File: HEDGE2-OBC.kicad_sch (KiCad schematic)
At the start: 36 parts, among them J1 SMA-J-P-X-RA-TH1, U1 ADP7158ARDZ-3.3-R7, U3 TXS0102QDCURQ1

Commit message: Arbitrary change for demo purposes
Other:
- note added: "arvitrary text"
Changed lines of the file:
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@@
+		)
+	)
+	(text "arvitrary text"
+		(exclude_from_sim no)
+		(at 119.634 144.526 0)
+		(effects
+			(font
+				(size 1.27 1.27)
+			)
 		)
 	)

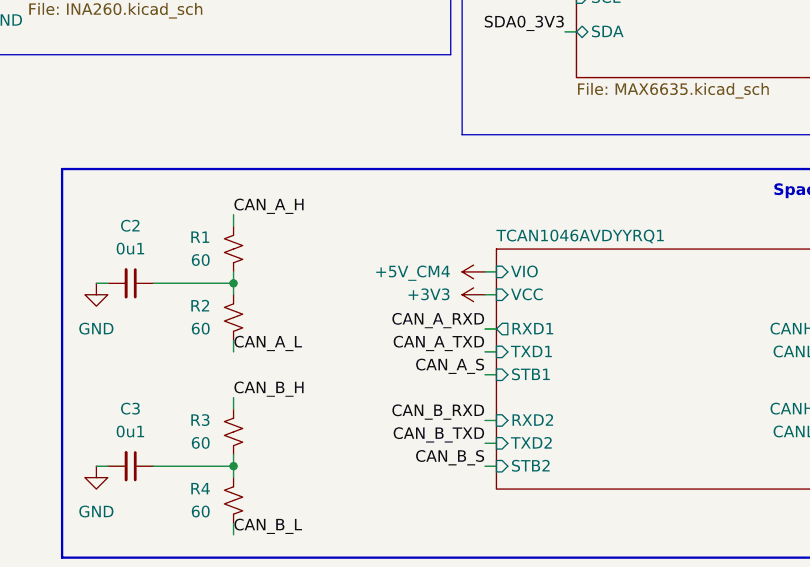
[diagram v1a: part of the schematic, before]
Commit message: Fix TCAN power supply swap
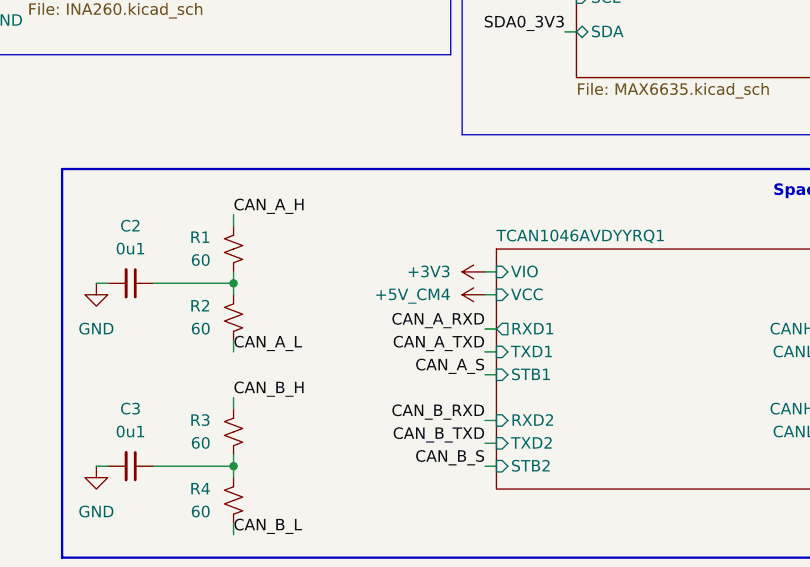
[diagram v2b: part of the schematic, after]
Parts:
- C1, C5, C6: DigiKey Part Number (none) -> 1276-1029-1-ND
- C7, C8: DigiKey Part Number (none) -> 720-GA0805Y104JXABT31GCT-ND
- MH1, MH2, MH3, MH4: now left out of the parts list
- R10, R11, R20, R21: DigiKey Part Number RMCF0805JT47K0CT-ND -> 541-4131-1-ND
- R5: DigiKey Part Number (none) -> 541-10.0KCCT-ND
- R6, R7: DigiKey Part Number 541-2.10KCCT-ND -> 541-1.00KCCT-ND
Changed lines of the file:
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@@
 			)
 		)
-		(property "DigiKey Part Number" "RMCF0805JT47K0CT-ND"
+		(property "DigiKey Part Number" "541-4131-1-ND "
 			(at 308.61 194.31 0)
 			(effects
@@
 			)
 		)
+		(property "DigiKey Part Number" "1276-1029-1-ND"
+			(at 123.19 251.46 0)
+			(effects
+				(font
+					(size 1.27 1.27)
+				)
+				(hide yes)
+			)
+		)
 		(pin "1"
 		)
@@
 	(symbol
 		(lib_id "power:+5V")
-		(at 163.83 95.25 90)
+		(at 163.83 97.79 90)
 		(unit 1)
 		(exclude_from_sim no)
@@
 		(on_board yes)
 		(dnp no)
-		(fields_autoplaced yes)
 		(property "Reference" "#PWR033"
-			(at 167.64 95.25 0)
+			(at 167.64 97.79 0)
 			(effects
 				(font
@@
 		)
 		(property "Value" "+5V_CM4"
-			(at 160.02 95.2499 90)
+			(at 160.02 97.7899 90)
 			(effects
 				(font
@@
 		)
 		(property "Footprint" ""
-			(at 163.83 95.25 0)
+			(at 163.83 97.79 0)
 			(effects
 				(font
@@
 		)
 		(property "Datasheet" ""
-			(at 163.83 95.25 0)
+			(at 163.83 97.79 0)
 			(effects
 				(font
@@
 		)
 		(property "Description" "Power symbol creates a global label with name \"+5V\""
-			(at 163.83 95.25 0)
+			(at 163.83 97.79 0)
 			(effects
 				(font
@@
 			)
 		)
-		(property "DigiKey Part Number" "541-2.10KCCT-ND"
+		(property "DigiKey Part Number" "541-1.00KCCT-ND "
 			(at 327.66 144.78 0)
 			(effects
@@
 			)
 		)
-		(property "DigiKey Part Number" "RMCF0805JT47K0CT-ND"
+		(property "DigiKey Part Number" "541-4131-1-ND "
 			(at 308.61 185.42 0)
 			(effects
@@
 		(unit 1)
 		(exclude_from_sim no)
-		(in_bom yes)
+		(in_bom no)
 		(on_board yes)
 		(dnp no)
@@
 			)
 		)
+		(property "DigiKey Part Number" "720-GA0805Y104JXABT31GCT-ND"
+			(at 276.86 177.8 0)
+			(effects
+				(font
+					(size 1.27 1.27)
+				)
+				(hide yes)
+			)
+		)
 		(pin "1"
 		)
@@
 			)
 		)
+		(property "DigiKey Part Number" "1276-1029-1-ND"
+			(at 114.3 254 0)
+			(effects
+				(font
+					(size 1.27 1.27)
+				)
+				(hide yes)
+			)
+		)
 		(pin "1"
 		)
@@
 			)
 		)
-		(property "DigiKey Part Number" "541-2.10KCCT-ND"
+		(property "DigiKey Part Number" "541-1.00KCCT-ND "
 			(at 327.66 137.16 0)
 			(effects
@@
 			)
 		)
-		(property "DigiKey Part Number" "RMCF0805JT47K0CT-ND"
+		(property "DigiKey Part Number" "541-4131-1-ND "
 			(at 308.61 212.09 0)
 			(effects
@@
 			)
 		)
+		(property "DigiKey Part Number" "1276-1029-1-ND"
+			(at 17.78 251.46 0)
+			(effects
+				(font
+					(size 1.27 1.27)
+				)
+				(hide yes)
+			)
+		)
 		(pin "2"
 		)
@@
 			)
 		)
+		(property "DigiKey Part Number" "720-GA0805Y104JXABT31GCT-ND"
+			(at 276.86 190.5 0)
+			(effects
+				(font
+					(size 1.27 1.27)
+				)
+				(hide yes)
+			)
+		)
 		(pin "1"
 		)
@@
 	(symbol
 		(lib_id "power:+3V3")
-		(at 163.83 97.79 90)
+		(at 163.83 95.25 90)
 		(unit 1)
 		(exclude_from_sim no)
@@
 		(on_board yes)
 		(dnp no)
-		(fields_autoplaced yes)
 		(property "Reference" "#PWR034"
-			(at 167.64 97.79 0)
+			(at 167.64 95.25 0)
 			(effects
 				(font
@@
 		)
 		(property "Value" "+3V3"
-			(at 160.02 97.7899 90)
+			(at 160.02 95.2499 90)
 			(effects
 				(font
@@
 		)
 		(property "Footprint" ""
-			(at 163.83 97.79 0)
+			(at 163.83 95.25 0)
 			(effects
 				(font
@@
 		)
 		(property "Datasheet" ""
-			(at 163.83 97.79 0)
+			(at 163.83 95.25 0)
 			(effects
 				(font
@@
 		)
 		(property "Description" "Power symbol creates a global label with name \"+3V3\""
-			(at 163.83 97.79 0)
+			(at 163.83 95.25 0)
 			(effects
 				(font
@@
 		(unit 1)
 		(exclude_from_sim no)
-		(in_bom yes)
+		(in_bom no)
 		(on_board yes)
 		(dnp no)
@@
 		(unit 1)
 		(exclude_from_sim no)
-		(in_bom yes)
+		(in_bom no)
 		(on_board yes)
 		(dnp no)
@@
 		(unit 1)
 		(exclude_from_sim no)
-		(in_bom yes)
+		(in_bom no)
 		(on_board yes)
 		(dnp no)
@@
 			)
 		)
+		(property "DigiKey Part Number" "541-10.0KCCT-ND "
+			(at 238.76 184.15 0)
+			(effects
+				(font
+					(size 1.27 1.27)
+				)
+				(hide yes)
+			)
+		)
 		(pin "1"
 		)
@@
 			)
 		)
-		(property "DigiKey Part Number" "RMCF0805JT47K0CT-ND"
+		(property "DigiKey Part Number" "541-4131-1-ND "
 			(at 308.61 203.2 0)
 			(effects

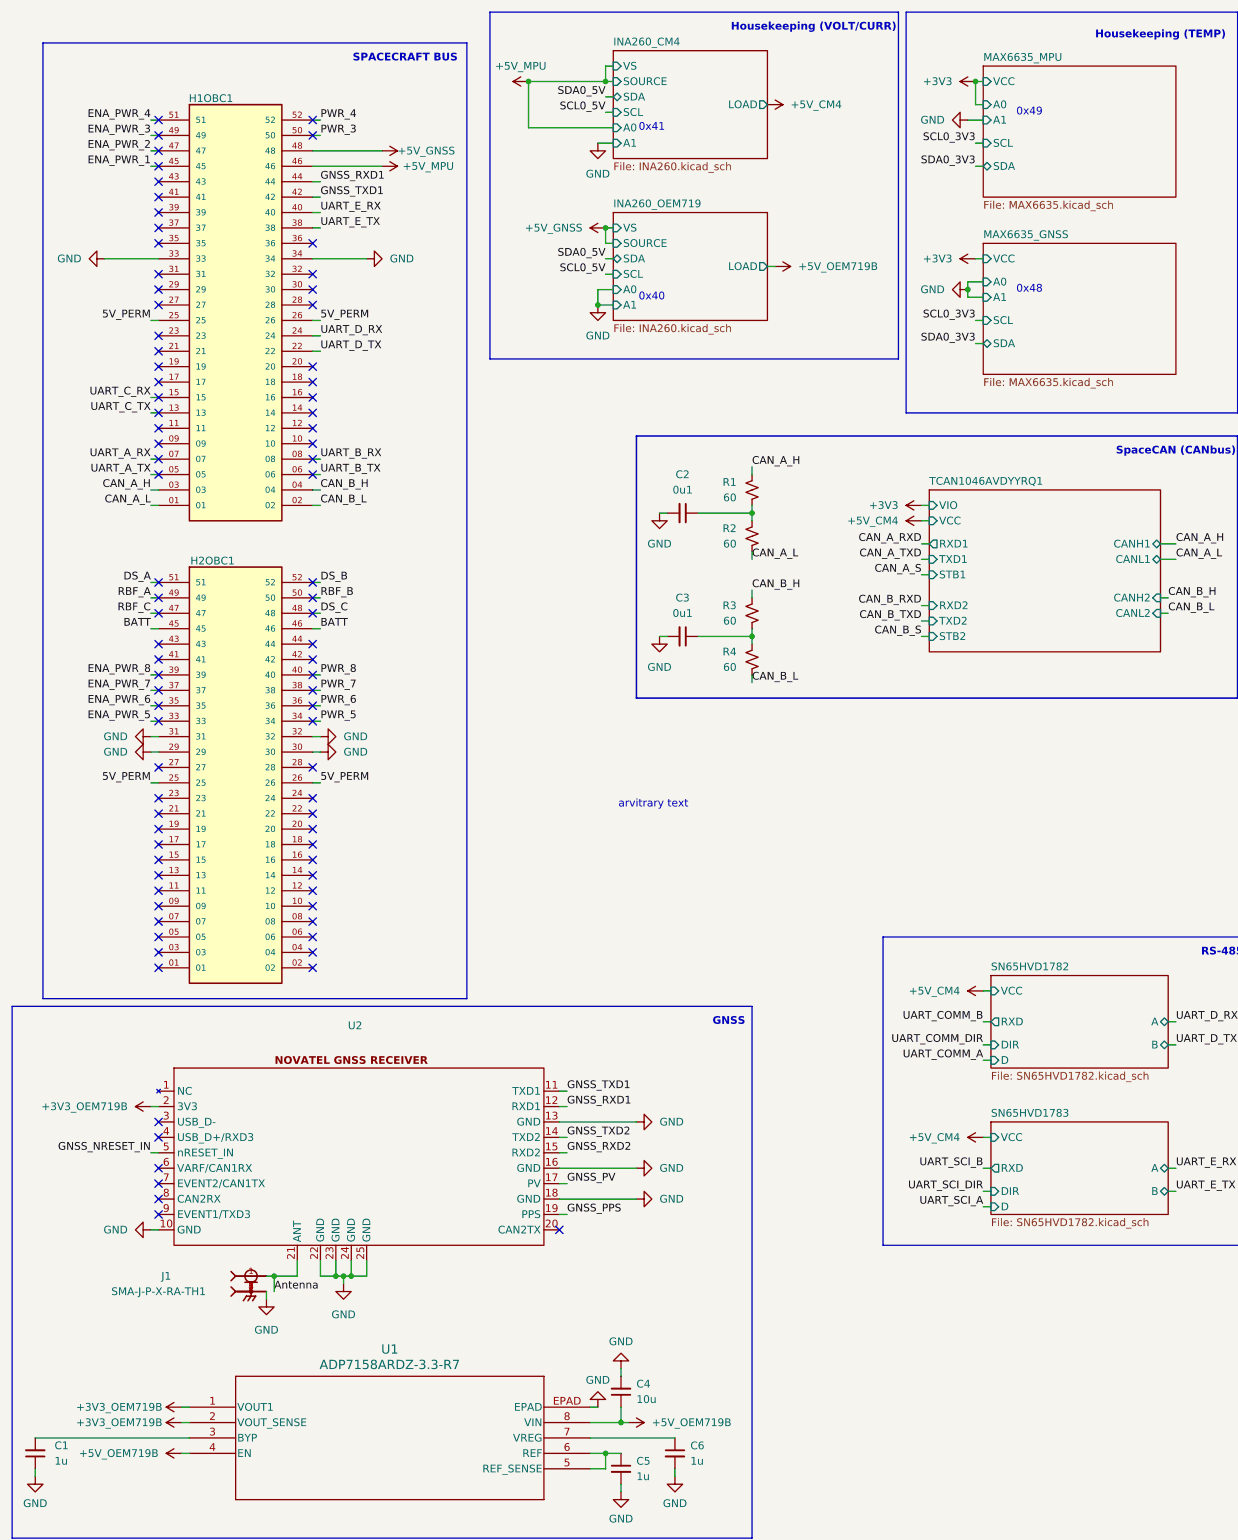
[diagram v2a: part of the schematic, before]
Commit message: Add cap to 3V3 LDO output; add solder jumpers; change 3V3 routing
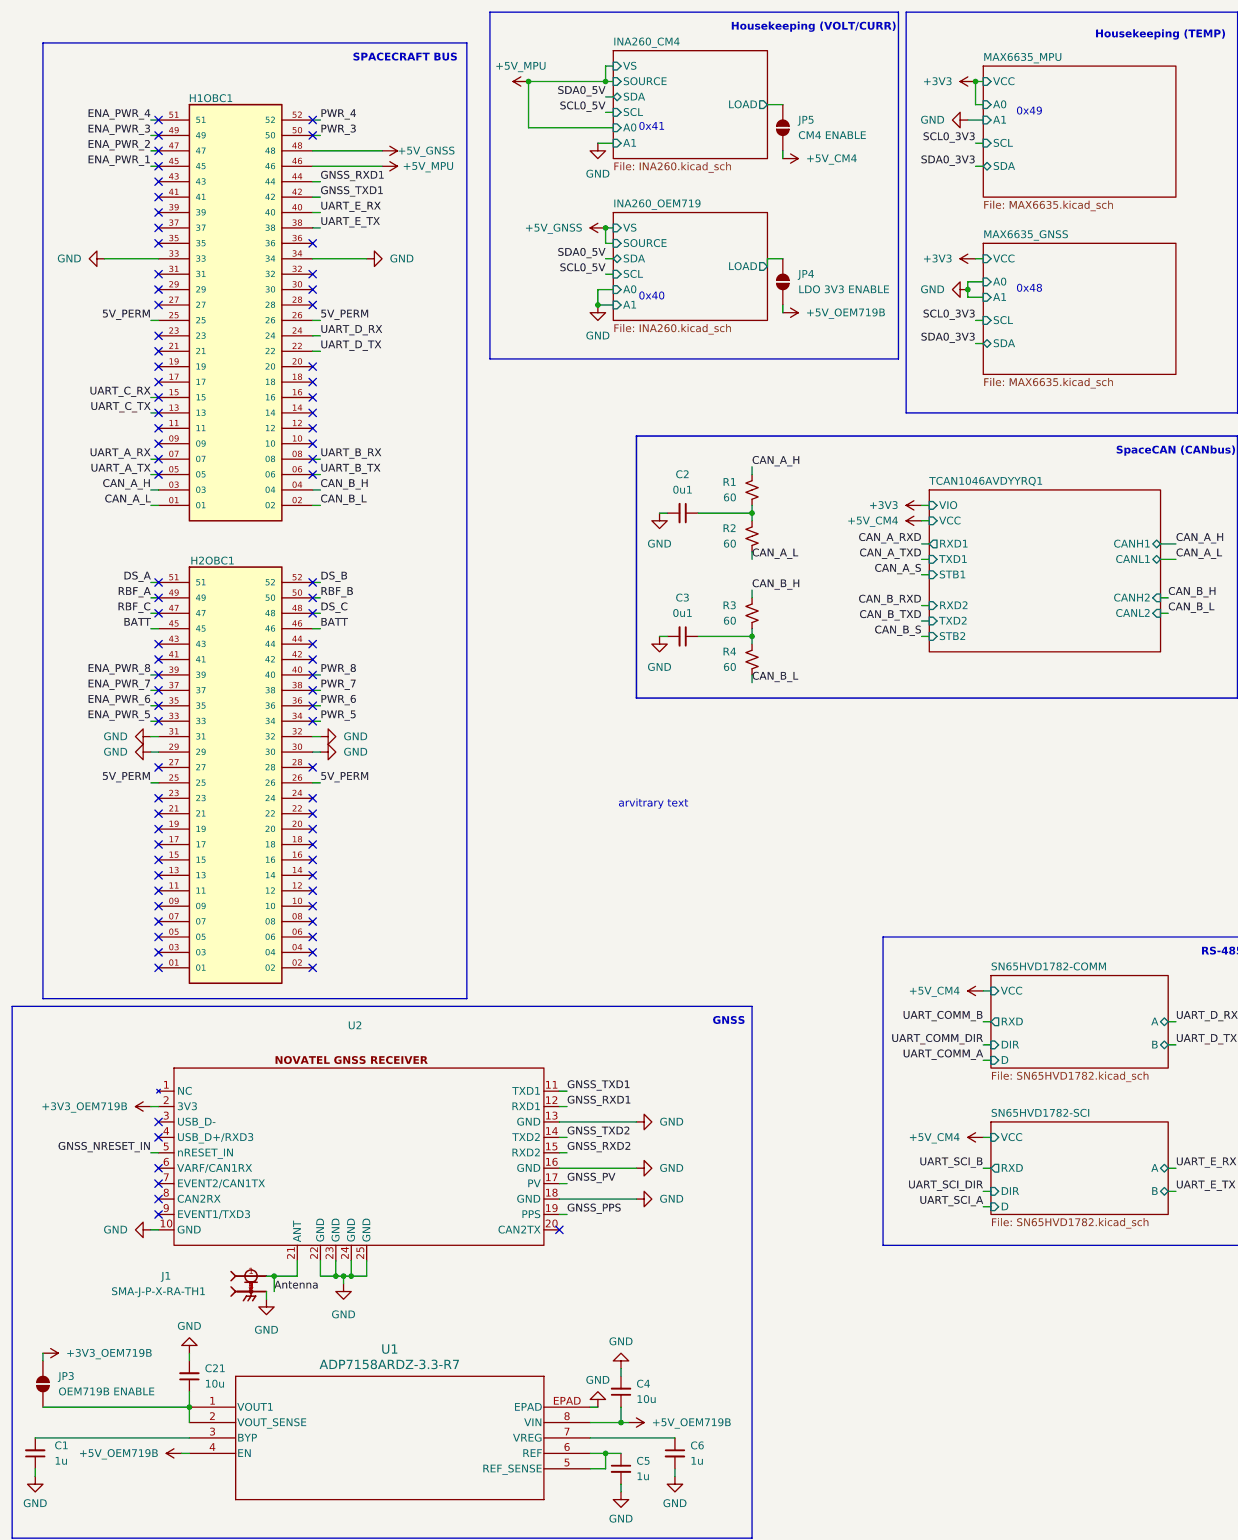
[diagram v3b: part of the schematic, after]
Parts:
- added C21: 10u, Capacitor_SMD:C_0805_2012Metric, symbol Device:C_Small
- added JP3: OEM719B ENABLE, Jumper:SolderJumper-2_P1.3mm_Open_RoundedPad1.0x1.5mm, symbol Jumper:SolderJumper_2_Open
- added JP4: LDO 3V3 ENABLE, Jumper:SolderJumper-2_P1.3mm_Open_RoundedPad1.0x1.5mm, symbol Jumper:SolderJumper_2_Open
- added JP5: CM4 ENABLE, Jumper:SolderJumper-2_P1.3mm_Open_RoundedPad1.0x1.5mm, symbol Jumper:SolderJumper_2_Open
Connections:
- net +3V3_OEM719B: now also JP3.2 (B); no longer U1.1 (VOUT1), U1.2 (VOUT_SENSE)
- net +5V_CM4: now also JP5.1 (A)
- net +5V_OEM719B: now also JP4.1 (A)
- net GND: now also C21.2
- new net: C21.1, JP3.1 (A), U1.1 (VOUT1), U1.2 (VOUT_SENSE)
- new net INA260_CM4/LOAD: JP5.2 (B)
- new net INA260_OEM719/LOAD: JP4.2 (B)
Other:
- sheet SN65HVD1782 renamed SN65HVD1782-COMM
- sheet SN65HVD1783 renamed SN65HVD1782-SCI

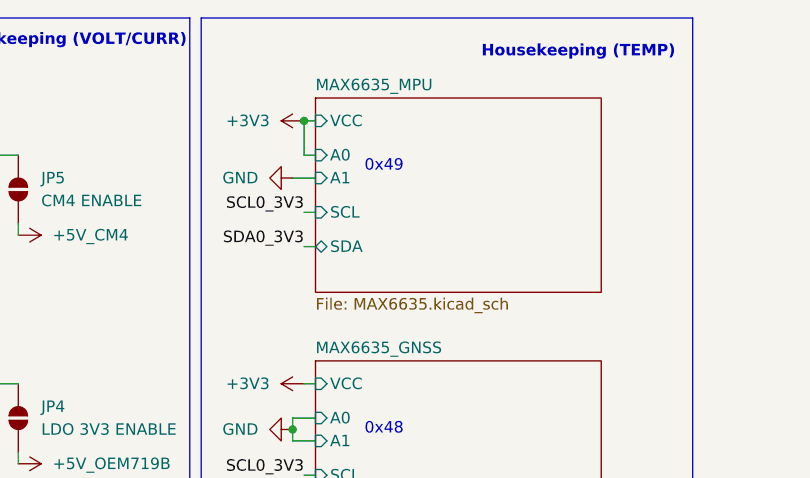
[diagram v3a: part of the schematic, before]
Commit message: Clean up CM4 routing
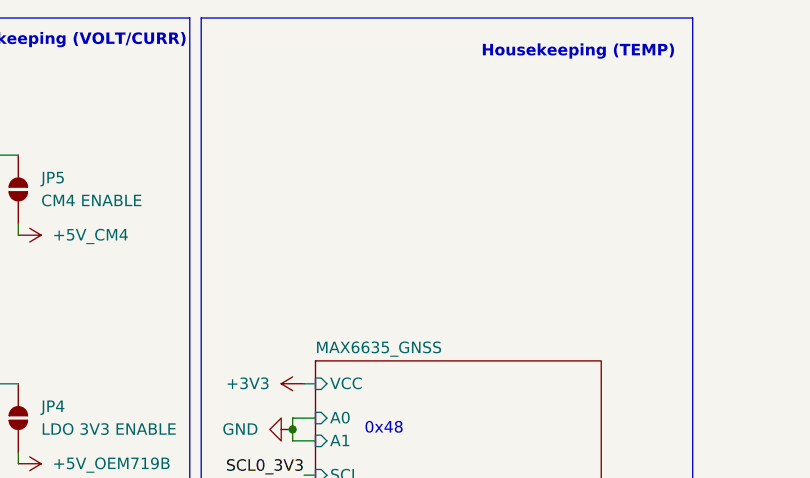
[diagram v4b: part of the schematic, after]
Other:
- removed sheet MAX6635_MPU
- note removed: "0x49"

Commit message: Add PCM5102A I2S audio output for APRS radio
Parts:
- removed JP1: WiFi_nDisable, Jumper:SolderJumper-2_P1.3mm_Open_RoundedPad1.0x1.5mm, symbol Jumper:SolderJumper_2_Open
- removed JP2: BT_nDisable, Jumper:SolderJumper-2_P1.3mm_Bridged2Bar_RoundedPad1.0x1.5mm, symbol Jumper:SolderJumper_2_Bridged
- removed R6, R7: 1k, Resistor_SMD:R_0805_2012Metric, symbol Device:R_Small_US
- added C10, C7: 2u2, Capacitor_SMD:C_0805_2012Metric, symbol Device:C_Small
- added C11, C12, C18, C19: 0u1, Capacitor_SMD:C_0805_2012Metric, symbol Device:C_Small
- added C17, C20, C8, C9: 10u, Capacitor_Tantalum_SMD:CP_EIA-2012-12_Kemet-R, symbol Device:C_Polarized_Small_US
- added C6: 2n2, Capacitor_SMD:C_0805_2012Metric, symbol Device:C_Small
- added R1: 470, Resistor_SMD:R_0805_2012Metric, symbol Device:R_Small_US
- added U3: SN74CBTLV3257PWR, SN74CBTLV3257PWR:PW16, symbol SN74CBTLV3257PWR:SN74CBTLV3257PWR
- added U4: PCM5102AQPWRQ1, PCM5102AQPWRQ1:PW20, symbol PCM5102AQPWRQ1:PCM5102AQPWRQ1
- renumbered C2 to C13, C3 to C14, C7 to C15, C8 to C16, C21 to C2, C4 to C3, C5 to C4, C6 to C5, JP3 to JP1, JP5 to JP2, JP4 to JP3, R11 to R10, R8 to R11, R9 to R12, R5 to R2, R1 to R3, R2 to R4, R3 to R5, R4 to R6, R20 to R7, R21 to R8, R10 to R9, U3 to U5
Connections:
- net UART_COMM_A is gone; now on net UART_TX_DMR: Module1.39 (GPIO8)
- net UART_COMM_DIR is gone; now on net PTT_DMR: Module1.41 (GPIO25)
- net BATT: now also H2OBC1.41, H2OBC1.42, H2OBC1.43, H2OBC1.44
- net CAN_A_S: now also Module1.47 (GPIO23); no longer Module1.49 (GPIO18)
- net GND: now also C11.2, C12.2, C17.2, C18.2, C19.2, C20.2, C6.2, C7.2, C8.2, C9.2, U4.10 (DEMP), U4.11 (FLT), U4.16 (FMT), U4.19 (DGND), U4.3 (CPGND), U4.9 (AGND)
- net UART_SCI_DIR: now also Module1.24 (GPIO26); no longer Module1.26 (GPIO19)
- net PCM_DOUT: now reaches Module1.25 (GPIO21)
- net PCM_DOUT: now also U4.14 (DIN)
- net DIN/CONFIG/DIO14_XB: now reaches H2OBC1.01
- net DOUT/DIO13_XB: now reaches H2OBC1.02
- net RTS/DIO6_XB: now reaches H2OBC1.03
- net CTS/DIO7_XB: now reaches H2OBC1.04
- net AD3/DIO3/SPI_SSEL_XB: now reaches H2OBC1.05
- net AD2/DIO2/SPI_CLK_XB: now reaches H2OBC1.06
- net DIO4/SPI_MOSI_XB: now reaches H2OBC1.07
- net DIO12/SPI_MISO_XB: now reaches H2OBC1.08
- net DTR/SLEEP_RQ/DIO8_XB: now reaches H2OBC1.09
- net AD1/DIO1/SPI_ATTN_XB: now reaches H2OBC1.10
- net ON_SLEEP/DIO9_XB: now reaches H2OBC1.11
- net DIO10/PWM0_XB: now reaches H2OBC1.12
- net RESET_XB: now reaches H2OBC1.13
- net DIO11/PWM1_XB: now reaches H2OBC1.14
- net AD0/DIO0_XB: now reaches H2OBC1.15
- net Associate/DIO5_XB: now reaches H2OBC1.16
- net NDTR_XB: now reaches H2OBC1.17
- net MIC_IN_DMR: now reaches H2OBC1.19
- net MIC_IN_DMR: now also C6.1, R1.1
- net LINE_OUT_DMR: now reaches H2OBC1.20
- net T/R_DMR: now reaches H2OBC1.21
- net PTT_DMR: now reaches H2OBC1.22
- net SPKEN_DMR: now reaches H2OBC1.23
- net CS_DMR: now reaches H2OBC1.24
- net HST_TXD_DMR: now reaches H2OBC1.27
- net UART_TX_DMR: now reaches H2OBC1.28
- net +3V3 renamed +3V3<CM4
- net +3V3<CM4: now also C11.1, C12.1, C17.1, C18.1, C8.1, C9.1, U4.1 (CPVDD), U4.17 (XSMT), U4.20 (DVDD), U4.8 (AVDD)
- net +3V3_OEM719B renamed +3V3>OEM719B
- removed net 5V_PERM: H1OBC1.25, H1OBC1.26, H2OBC1.25, H2OBC1.26
- net DS_A: no longer names the net of H2OBC1.51
- net DS_B: no longer names the net of H2OBC1.52
- net DS_C: no longer names the net of H2OBC1.48
- net ENA_PWR_1: no longer names the net of H1OBC1.45
- net ENA_PWR_2: no longer names the net of H1OBC1.47
- net ENA_PWR_3: no longer names the net of H1OBC1.49
- net ENA_PWR_4: no longer names the net of H1OBC1.51
- net PWR_3: no longer names the net of H1OBC1.50
- net PWR_4: no longer names the net of H1OBC1.52
- net RBF_A: no longer names the net of H2OBC1.49
- net RBF_B: no longer names the net of H2OBC1.50
- net RBF_C: no longer names the net of H2OBC1.47
- net UART_A_RX: no longer names the net of H1OBC1.07
- net UART_A_TX: no longer names the net of H1OBC1.05
- net UART_B_RX: no longer names the net of H1OBC1.08
- net UART_B_TX: no longer names the net of H1OBC1.06
- net UART_COMM_B renamed UART_RX_DMR
- net UART_RX_DMR: now also H2OBC1.26
- net UART_C_RX: no longer names the net of H1OBC1.15
- net UART_C_TX: no longer names the net of H1OBC1.13
- net UART_D_RX: no longer names the net of H1OBC1.24
- net UART_D_TX: no longer names the net of H1OBC1.22
- new net: C10.1, U4.2 (CAPP)
- new net: C10.2, U4.4 (CAPM)
- new net: C7.1, U4.5 (VNEG)
- new net HST_RXD_DMR: H2OBC1.25
- new net LDOO: C19.1, C20.1, U4.18 (LDOO)
- new net OUTL: R1.2, U4.6 (OUTL)
- new net PCM_CLK: Module1.49 (GPIO18), U4.13 (BCK)
- new net PCM_FS: Module1.26 (GPIO19), U4.15 (LRCK)
- no-connect marks 203 -> 179
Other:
- removed sheet SN65HVD1782-COMM
- note removed: "arvitrary text"
- moved on the sheet: C1, C13, C14, C15, C16, C2, C3, C4, C5, D1, D2, H1OBC1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
